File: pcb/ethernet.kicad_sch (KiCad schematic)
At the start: 40 parts, among them J4 RJ45_Hanrun_HR911105A_Horizon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, U9 W5500, Y1 25MHz

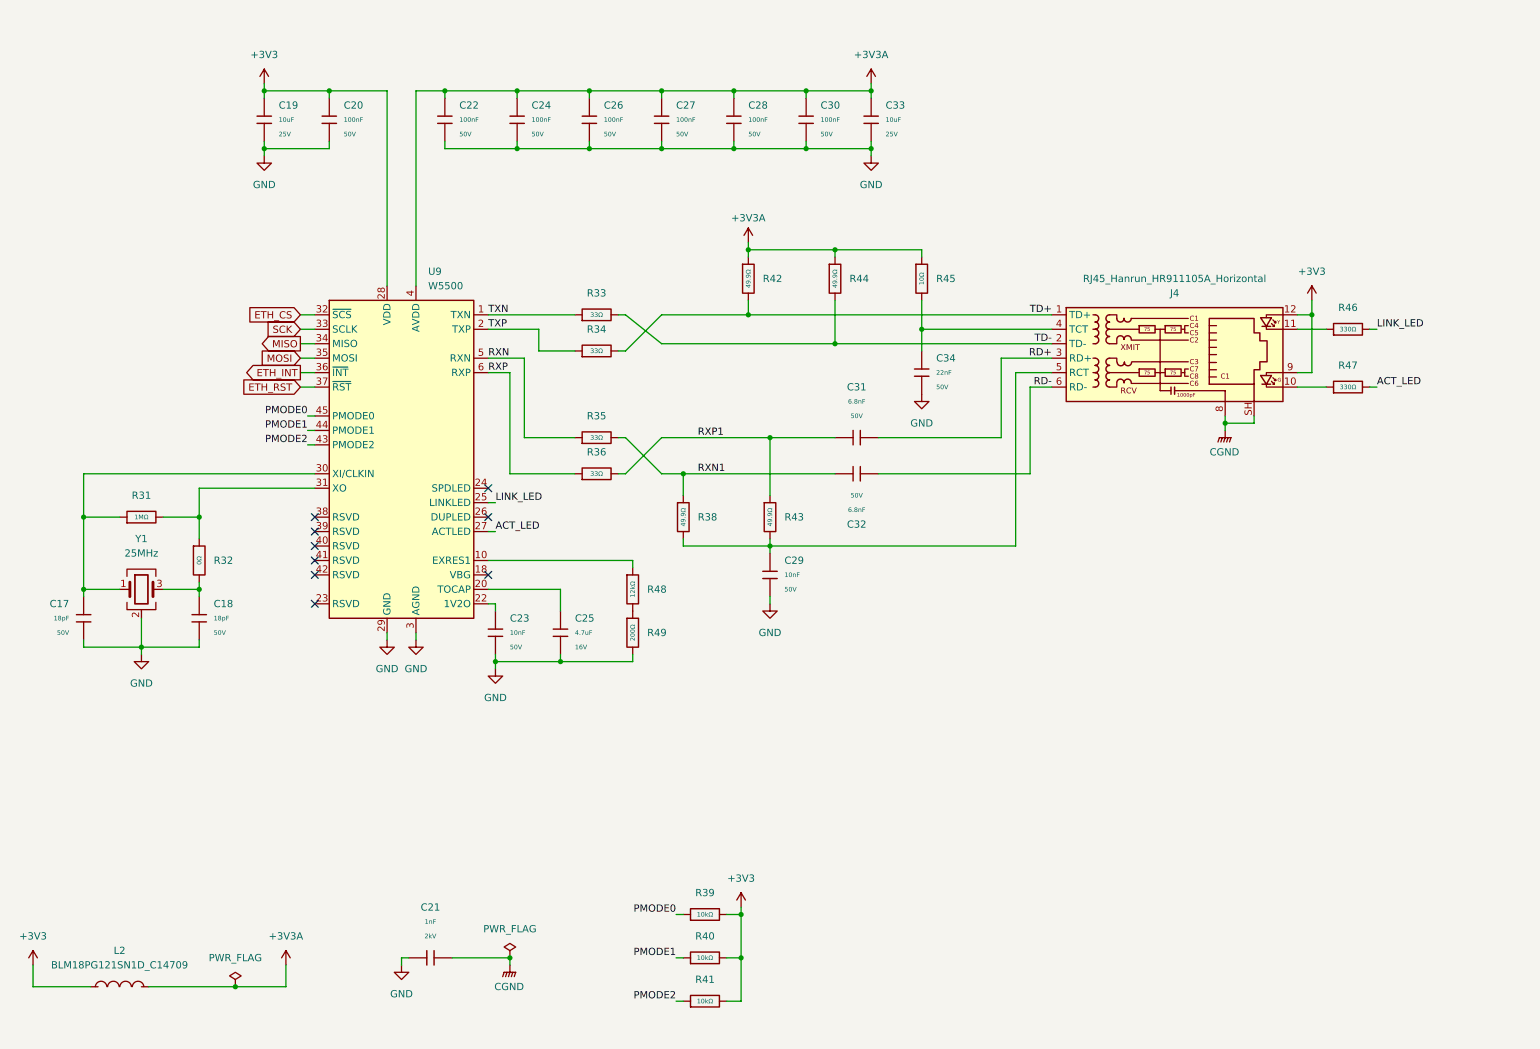
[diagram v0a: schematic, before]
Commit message: sch: clean up ethernet schematic
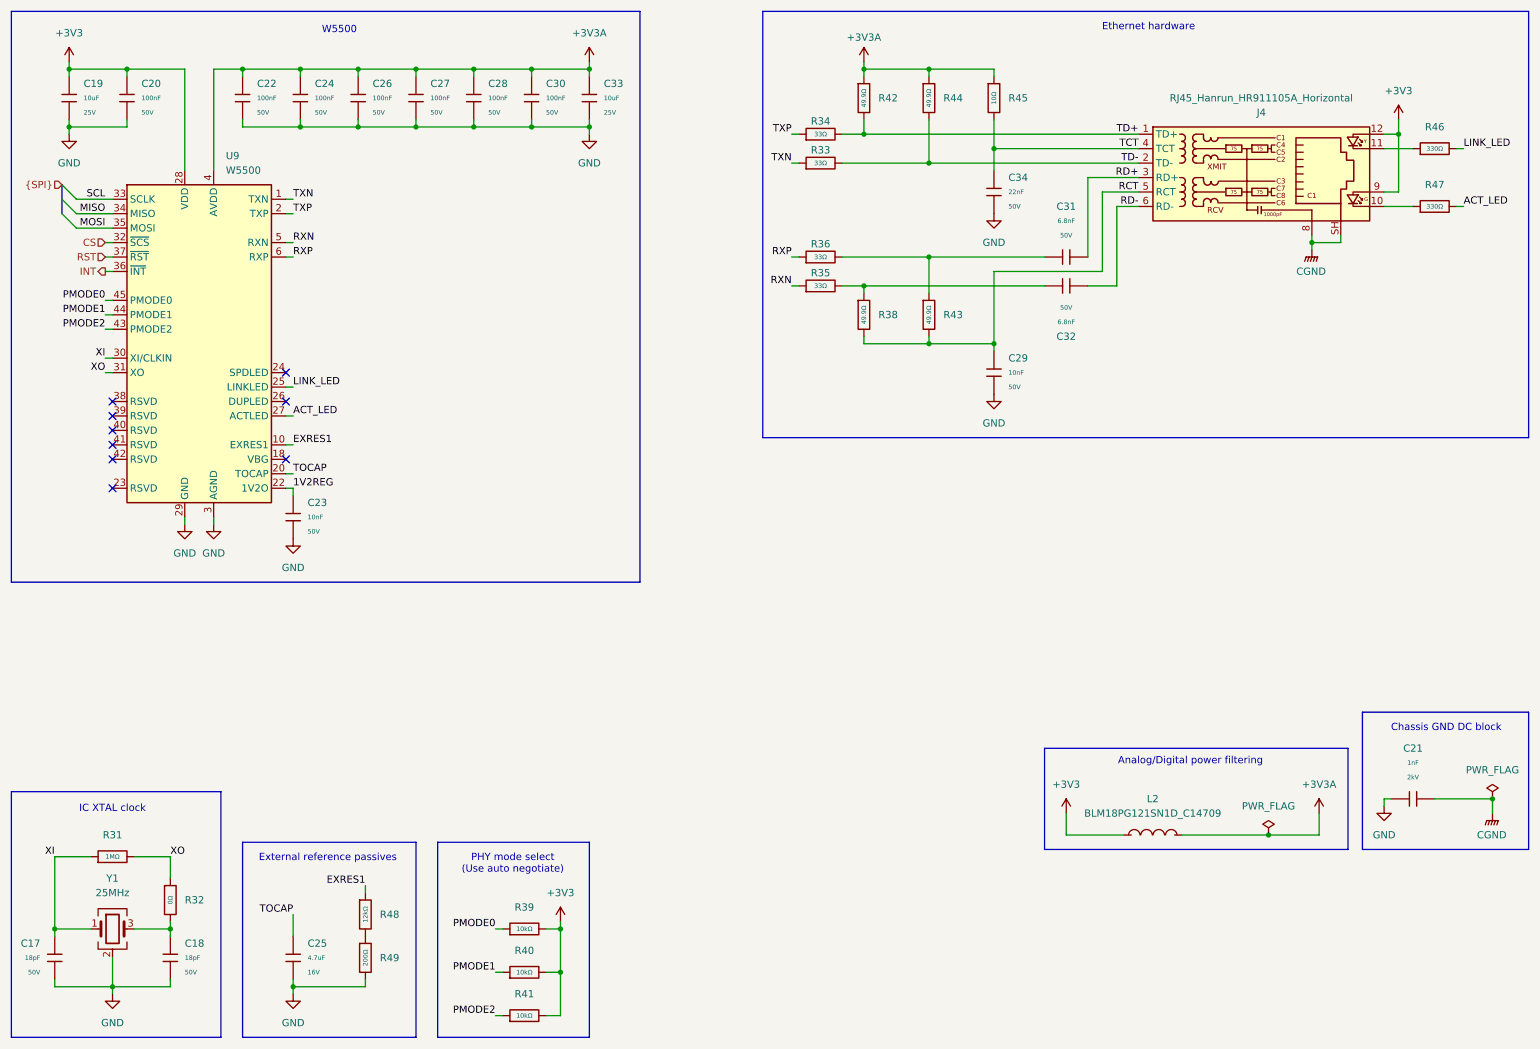
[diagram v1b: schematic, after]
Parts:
- U9: footprint EasyEDA:LQFP-48_L7.0-W7.0-P0.50-LS9.0-BL -> Package_QFP:LQFP-48_7x7mm_P0.5mm; symbol Interface_Ethernet:W5500 -> custom_symbols:W5500
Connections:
- net TCT: now reaches C34.1, J4.4 (TCT), R45.2
- net RCT: now reaches C29.1, J4.5 (RCT), R38.2, R43.2
- net EXRES1: now reaches R48.1, U9.10 (EXRES1)
- net XI: now reaches C17.1, R31.1, U9.30 (XI/CLKIN), Y1.1
- net XO: now reaches R31.2, R32.1, U9.31 (XO)
- net 1V2REG: now reaches C23.1, U9.22 (1V2O)
- net TOCAP: now reaches C25.1, U9.20 (TOCAP)
- net ETH_CS renamed CS
- net ETH_INT renamed INT
- net ETH_RST renamed RST
- net RXN1: no longer names the net of C32.1, R35.2, R38.1
- net RXP1: no longer names the net of C31.1, R36.2, R43.1
- net SCK renamed SCL
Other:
- note added: "Analog/Digital power filtering"
- note added: "Chassis GND DC block"
- note added: "Ethernet hardware"
- note added: "External reference passives"
- note added: "IC XTAL clock"
- note added: "PHY mode select (Use auto negotiate)"
- note added: "W5500"
- moved on the sheet: C17, C18, C19, C20, C21, C22, C23, C24, C25, C26, C27, C28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

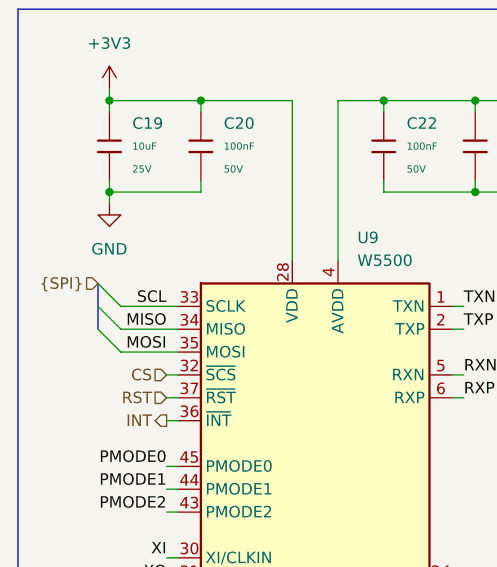
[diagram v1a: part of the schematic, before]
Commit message: sch: remove usb power and clean up mcu sheet
Fixes #15
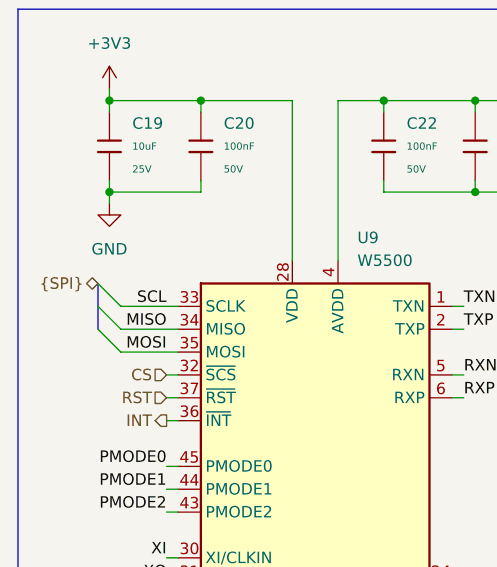
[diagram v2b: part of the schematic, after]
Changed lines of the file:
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@@
 	)
 	(hierarchical_label "{SPI}"
-		(shape input)
+		(shape bidirectional)
 		(at 24.13 45.72 180)
 		(effects

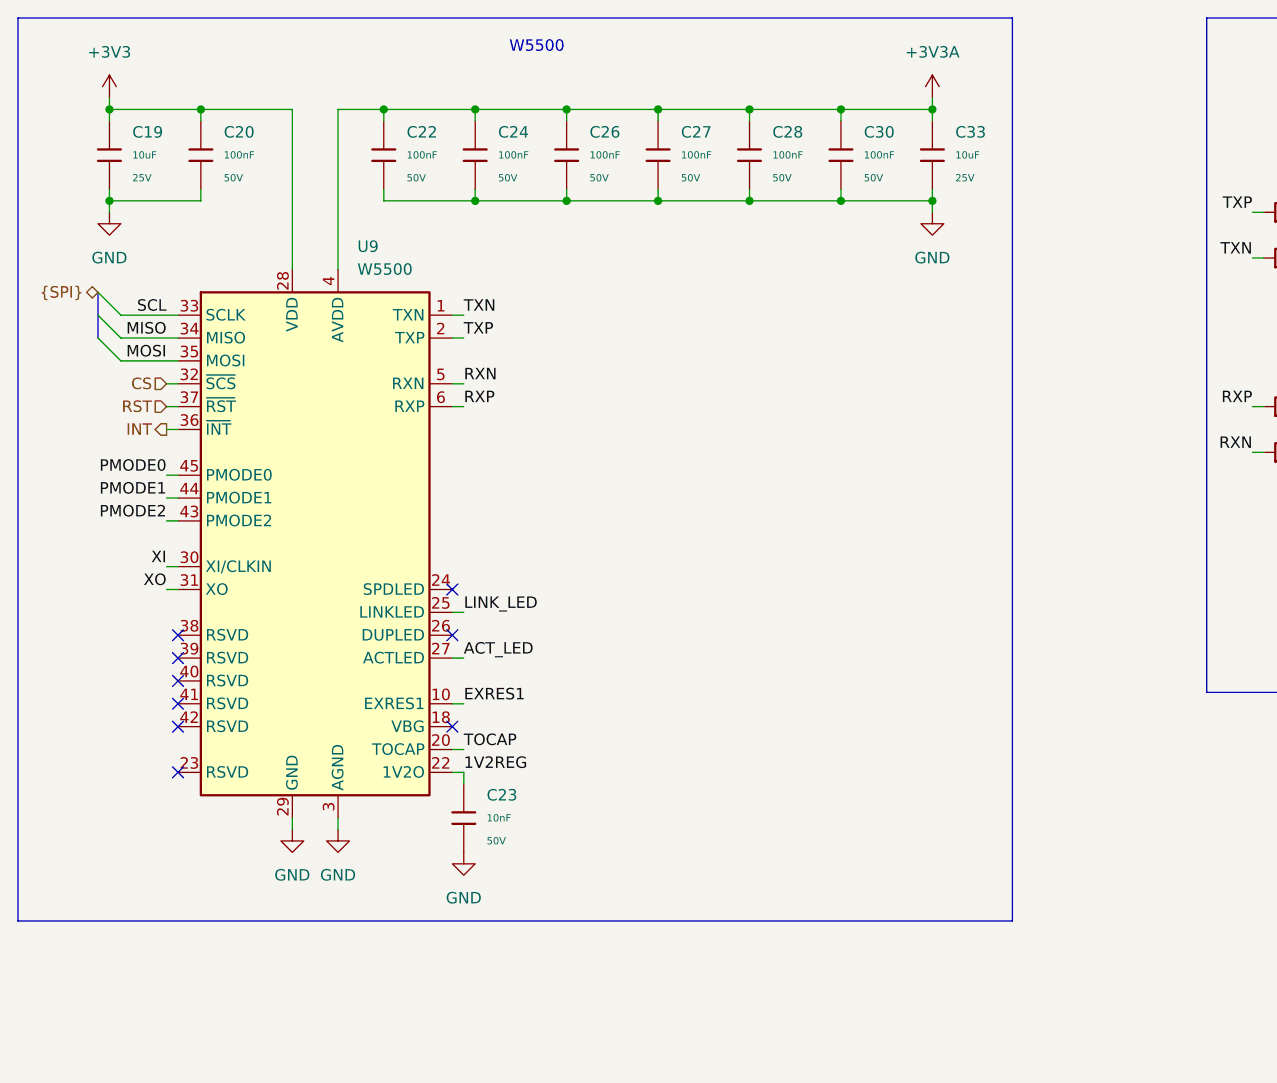
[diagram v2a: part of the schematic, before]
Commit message: sch: replace mcu and clean up schematic
Fixes #27
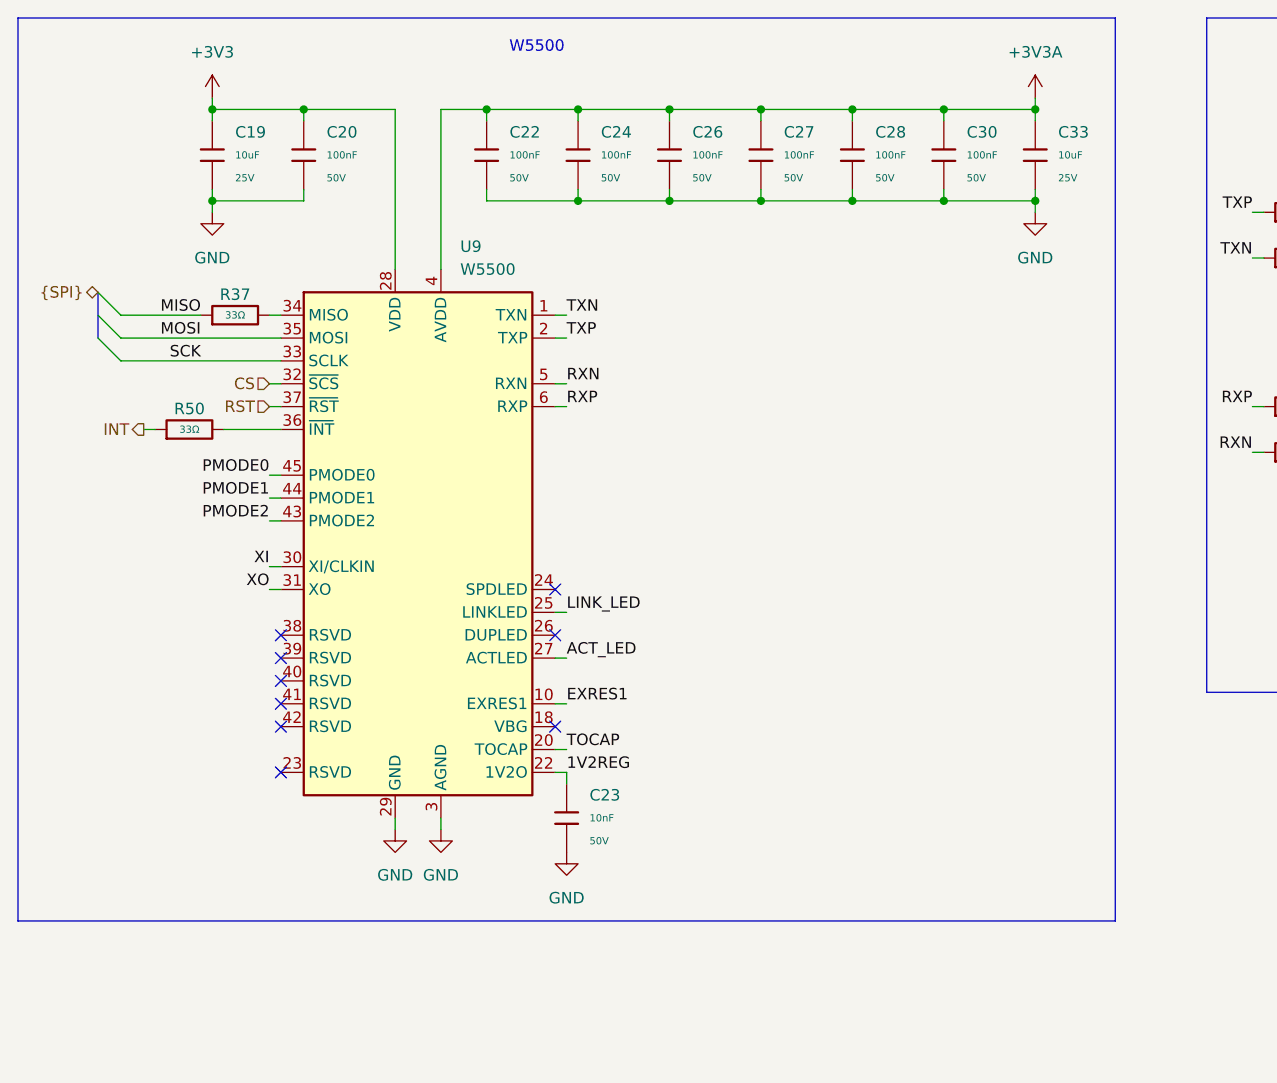
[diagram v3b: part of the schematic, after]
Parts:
- added R37, R50: 33Ω, PCM_JLCPCB:R_0603, symbol PCM_JLCPCB-Resistors:0603,33Ω
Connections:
- net INT: now also R50.1; no longer U9.36 (~{INT})
- net MISO: now also R37.1; no longer U9.34 (MISO)
- net SCL renamed SCK
- new net: R37.2, U9.34 (MISO)
- new net: R50.2, U9.36 (~{INT})
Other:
- moved on the sheet: C19, C20, C22, C23, C24, C26, C27, C28, C30, C33, U9

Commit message: sch: switch to vertical ethernet jack
Replace the original right-angled ethernet connector with a vertical one to make routing and placement easier. Relates to #42
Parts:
- removed J4: RJ45_Hanrun_HR911105A_Horizontal, EasyEDA:RJ45-TH_HR911105A, symbol Connector:RJ45_Hanrun_HR911105A_Horizontal
- added D2: HR915310A, EasyEDA:RJ45-TH_HR915310A, symbol EasyEDA:HR915310A
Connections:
- net +3V3: now also D2.12, D2.9
- net CGND: now also D2.8, D2.SH
- net RCT: now also D2.5 (RCT)
- net RD+: now also D2.6 (RD+)
- net RD-: now also D2.7 (RD-)
- net TCT: now also D2.3 (TCT)
- net TD+: now also D2.1 (TD+)
- net TD-: now also D2.2 (TD-)
- net at R46.1: now also D2.11
- net at R47.1: now also D2.10
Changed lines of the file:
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@@
+	)
+	(symbol
+		(lib_id "EasyEDA:HR915310A")
+		(at 234.95 44.45 0)
+		(unit 1)
+		(body_style 1)
+		(exclude_from_sim no)
+		(in_bom yes)
+		(on_board yes)
+		(in_pos_files yes)
+		(dnp no)
+		(property "Reference" "D2"
+			(at 235.204 30.734 0)
+			(show_name no)
+			(do_not_autoplace no)
+			(effects
+				(font
+					(size 1.27 1.27)
+				)
+			)
+		)
+		(property "Value" "HR915310A"
+			(at 235.204 33.274 0)
+			(show_name no)
+			(do_not_autoplace no)
+			(effects
+				(font
+					(size 1.27 1.27)
+				)
+			)
+		)
+		(property "Footprint" "EasyEDA:RJ45-TH_HR915310A"
+			(at 234.95 72.39 0)
+			(hide yes)
+			(show_name no)
+			(do_not_autoplace no)
+			(effects
+				(font
+					(size 1.27 1.27)
+				)
+			)
+		)
+		(property "Datasheet" "https://www.lcsc.com/datasheet/C2760326.pdf"
+			(at 234.95 74.93 0)
+			(hide yes)
+			(show_name no)
+			(do_not_autoplace no)
+			(effects
+				(font
+					(size 1.27 1.27)
+				)
+			)
+		)
+		(property "Description" ""
+			(at 234.95 44.45 0)
+			(hide yes)
+			(show_name no)
+			(do_not_autoplace no)
+			(effects
+				(font
+					(size 1.27 1.27)
+				)
+			)
+		)
+		(property "Manufacturer" "HANRUN(汉仁)"
+			(at 234.95 77.47 0)
+			(hide yes)
+			(show_name no)
+			(do_not_autoplace no)
+			(effects
+				(font
+					(size 1.27 1.27)
+				)
+			)
+		)
+		(property "MPN" "HR915310A"
+			(at 234.95 80.01 0)
+			(hide yes)
+			(show_name no)
+			(do_not_autoplace no)
+			(effects
+				(font
+					(size 1.27 1.27)
+				)
+			)
+		)
+		(property "LCSC Part" "C2760326"
+			(at 234.95 82.55 0)
+			(hide yes)
+			(show_name no)
+			(do_not_autoplace no)
+			(effects
+				(font
+					(size 1.27 1.27)
+				)
+			)
+		)
+		(pin "11"
+		)
+		(pin "10"
+		)
+		(pin "12"
+		)
+		(pin "5"
+		)
+		(pin "8"
+		)
+		(pin "2"
+		)
+		(pin "1"
+		)
+		(pin "4"
+		)
+		(pin "3"
+		)
+		(pin "SH"
+		)
+		(pin "7"
+		)
+		(pin "6"
+		)
+		(pin "9"
+		)
+		(instances
+			(project "EveningStar"
+				(path "/4c61f5a2-f8d4-462a-9bc3-d74437d30372/561d5dbe-6020-48c7-be42-1a6149a1119b"
+					(reference "D2")
+					(unit 1)
+				)
+			)
+		)
 	)
 	(symbol
@@
 					(unit 1)
 				)
-			)
-		)
-	)
-	(symbol
-		(lib_id "Connector:RJ45_Hanrun_HR911105A_Horizontal")
-		(at 233.68 44.45 0)
-		(unit 1)
-		(body_style 1)
-		(exclude_from_sim no)
-		(in_bom yes)
-		(on_board yes)
-		(in_pos_files yes)
-		(dnp no)
-		(property "Reference" "J4"
-			(at 234.95 33.02 0)
-			(show_name no)
-			(do_not_autoplace no)
-			(effects
-				(font
-					(size 1.27 1.27)
-				)
-			)
-		)
-		(property "Value" "RJ45_Hanrun_HR911105A_Horizontal"
-			(at 234.95 30.48 0)
-			(show_name no)
-			(do_not_autoplace no)
-			(effects
-				(font
-					(size 1.27 1.27)
-				)
-			)
-		)
-		(property "Footprint" "EasyEDA:RJ45-TH_HR911105A"
-			(at 233.68 31.75 0)
-			(hide yes)
-			(show_name no)
-			(do_not_autoplace no)
-			(effects
-				(font
-					(size 1.27 1.27)
-				)
-			)
-		)
-		(property "Datasheet" "https://lcsc.com/product-detail/RJ45_RJ45-LED_C12074.html"
-			(at 233.68 29.21 0)
-			(hide yes)
-			(show_name no)
-			(do_not_autoplace no)
-			(effects
-				(font
-					(size 1.27 1.27)
-				)
-			)
-		)
-		(property "Description" "1 Port RJ45 Magjack Connector Through Hole 10/100 Base-T, AutoMDIX"
-			(at 233.68 44.45 0)
-			(hide yes)
-			(show_name no)
-			(do_not_autoplace no)
-			(effects
-				(font
-					(size 1.27 1.27)
-				)
-			)
-		)
-		(property "MPN" "HR911105A"
-			(at 233.68 44.45 0)
-			(hide yes)
-			(show_name no)
-			(do_not_autoplace no)
-			(effects
-				(font
-					(size 1.27 1.27)
-				)
-			)
-		)
-		(property "LCSC Part" "C12074"
-			(at 233.68 44.45 0)
-			(hide yes)
-			(show_name no)
-			(do_not_autoplace no)
-			(effects
-				(font
-					(size 1.27 1.27)
-				)
-			)
-		)
-		(property "Sim.Pins" ""
-			(at 233.68 44.45 0)
-			(hide yes)
-			(show_name no)
-			(do_not_autoplace no)
-			(effects
-				(font
-					(size 1.27 1.27)
-				)
-			)
-		)
-		(property "KLC_S3.3" ""
-			(at 233.68 44.45 0)
-			(hide yes)
-			(show_name no)
-			(do_not_autoplace no)
-			(effects
-				(font
-					(size 1.27 1.27)
-				)
-			)
-		)
-		(property "KLC_S4.1" ""
-			(at 233.68 44.45 0)
-			(hide yes)
-			(show_name no)
-			(do_not_autoplace no)
-			(effects
-				(font
-					(size 1.27 1.27)
-				)
-			)
-		)
-		(pin "5"
-		)
-		(pin "4"
-		)
-		(pin "1"
-		)
-		(pin "10"
-		)
-		(pin "3"
-		)
-		(pin "9"
-		)
-		(pin "6"
-		)
-		(pin "SH"
-		)
-		(pin "11"
-		)
-		(pin "7"
-		)
-		(pin "12"
-		)
-		(pin "8"
-		)
-		(pin "2"
-		)
-		(instances
-			(project "EveningStar"
-				(path "/4c61f5a2-f8d4-462a-9bc3-d74437d30372/561d5dbe-6020-48c7-be42-1a6149a1119b"
-					(reference "J4")
-					(unit 1)
-				)
